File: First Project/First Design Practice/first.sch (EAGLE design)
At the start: 6 parts, among them U1 ARDUINOR3-BPLACE

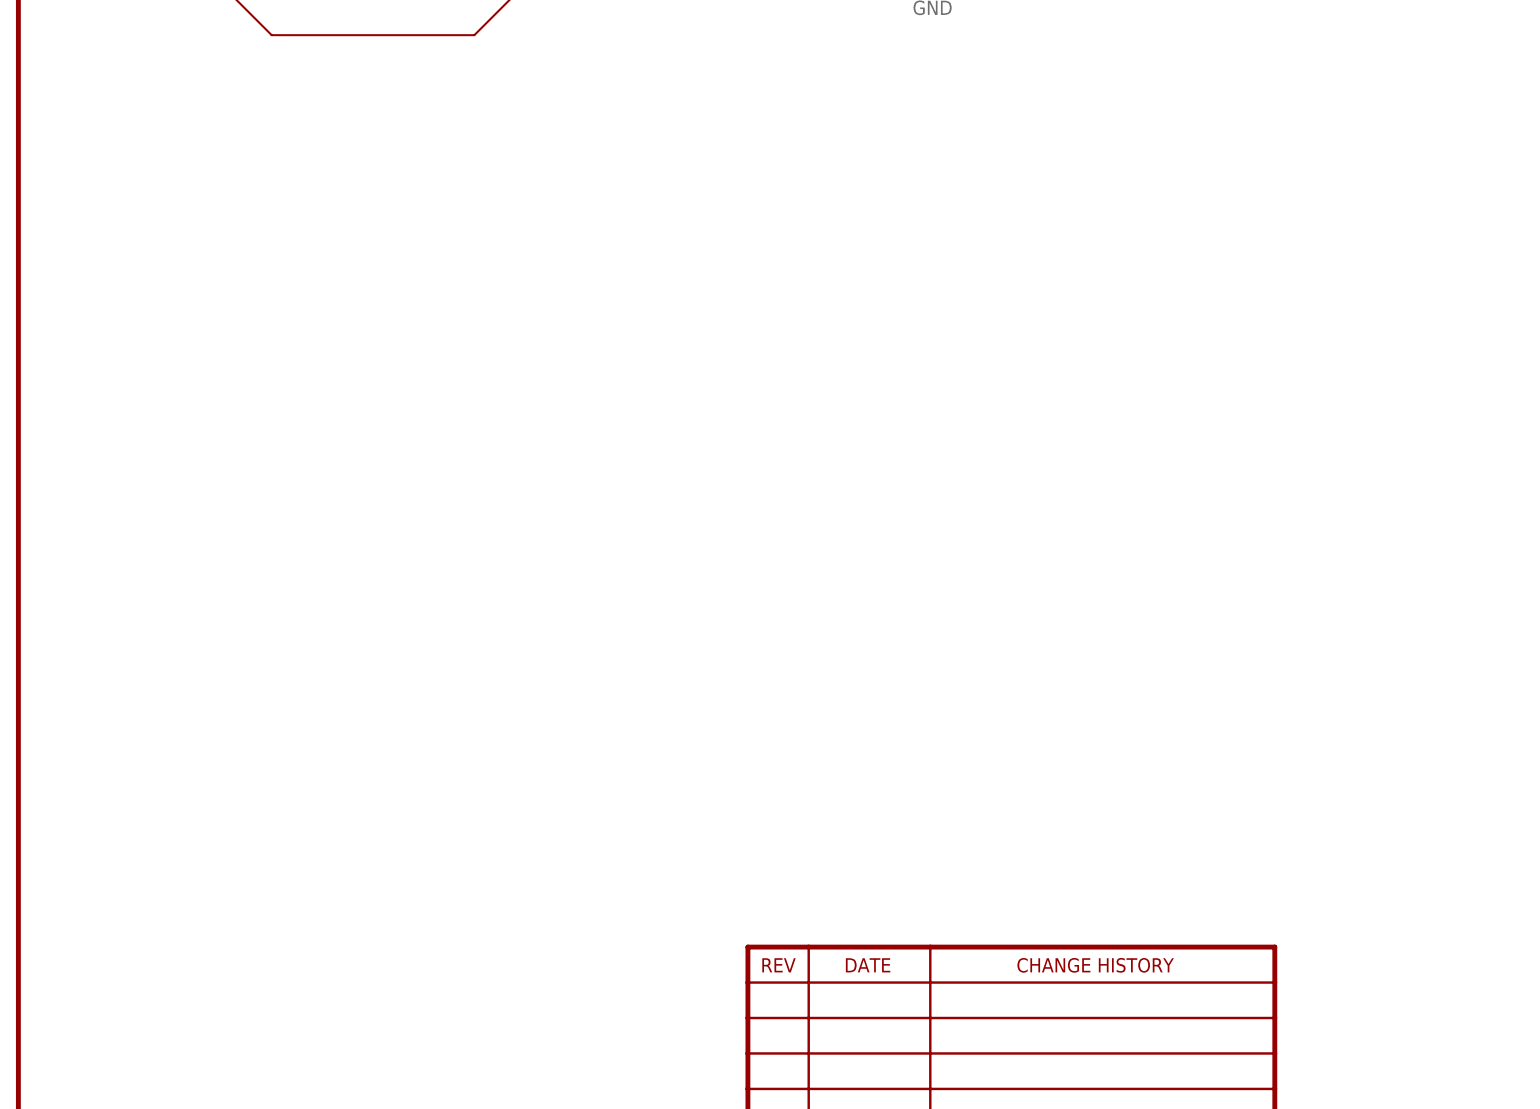
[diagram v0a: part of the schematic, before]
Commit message: Added Experimental Boards/ Gravity Board/ Home Automation Boards
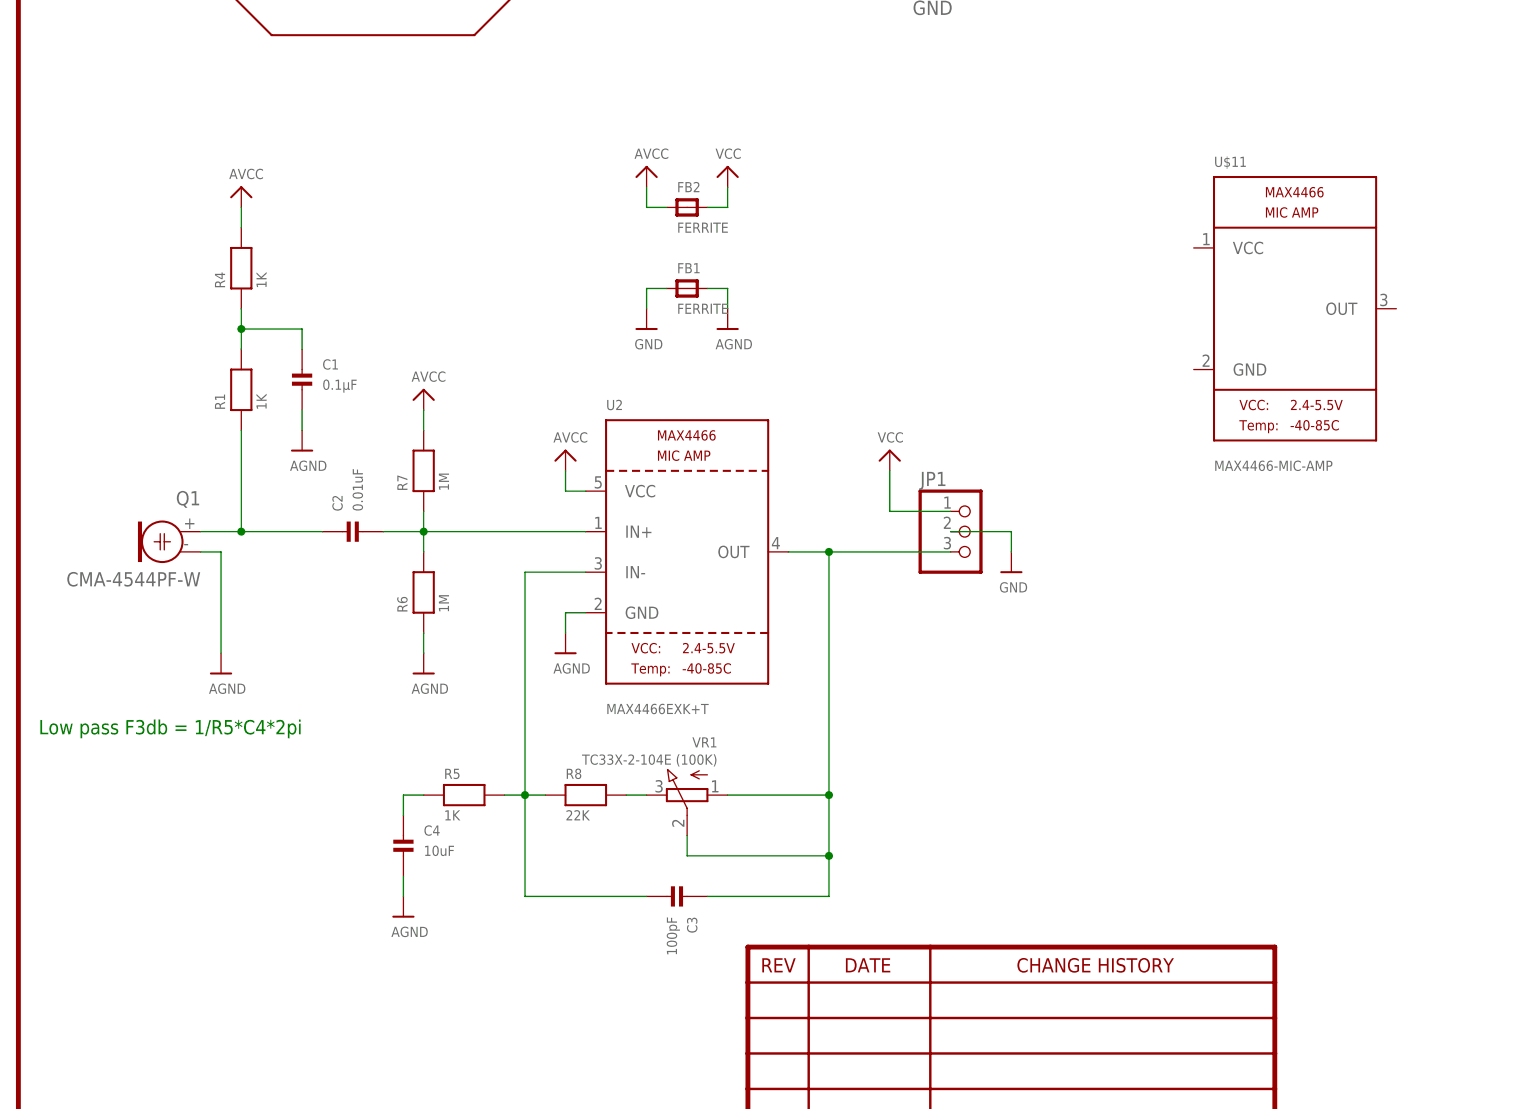
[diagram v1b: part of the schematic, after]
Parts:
- added C1: 0.1µF, microbuilder:CAP_CERAMIC0805
- added C2: 0.01uF, microbuilder:CAP_CERAMIC0805
- added C3: 100pF, microbuilder:CAP_CERAMIC0805
- added C4: 10uF, microbuilder:CAP_CERAMIC0805
- added FB1, FB2: FERRITE, microbuilder:FERRITE0805
- added JP1: (no value), microbuilder:HEADER-1X376MIL
- added Q1: CMA-4544PF-W, microbuilder:ELECTRET
- added R1, R4, R5: 1K, microbuilder:RESISTOR0805
- added R6, R7: 1M, microbuilder:RESISTOR0805
- added R8: 22K, microbuilder:RESISTOR0805
- added U$11: MAX4466-MIC-AMP, untitled:MAX4466-MIC-AMP
- added U2: MAX4466EXK+T, microbuilder:MAX4466""
- added VR1: TC33X-2-104E (100K), microbuilder:TRIMPOTTC33X-2
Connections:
- new net AGND: C1.P$2, C4.P$2, FB1.P$2, Q1.1, R6.1, U2.GND
- new net AVCC: FB2.P$1, R4.2, R7.2, U2.VCC
- new net N$10: C4.P$1, R5.1
- new net N$11: R8.2, VR1.E
- new net N$4: C2.P$1, Q1.2, R1.1
- new net N$6: C1.P$1, R1.2, R4.1
- new net N$7: C2.P$2, R6.2, R7.1, U2.IN+
- new net N$8: C3.P$1, JP1.3, U2.OUT, VR1.A, VR1.S
- new net N$9: C3.P$2, R5.2, R8.1, U2.IN-
- new net VCC: FB2.P$2, JP1.1
- net GND: now also FB1.P$1, JP1.2
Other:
- note added: "Low pass F3db = 1/R5*C4*2pi"
